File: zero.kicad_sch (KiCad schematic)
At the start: 11 parts, among them U1 Pico

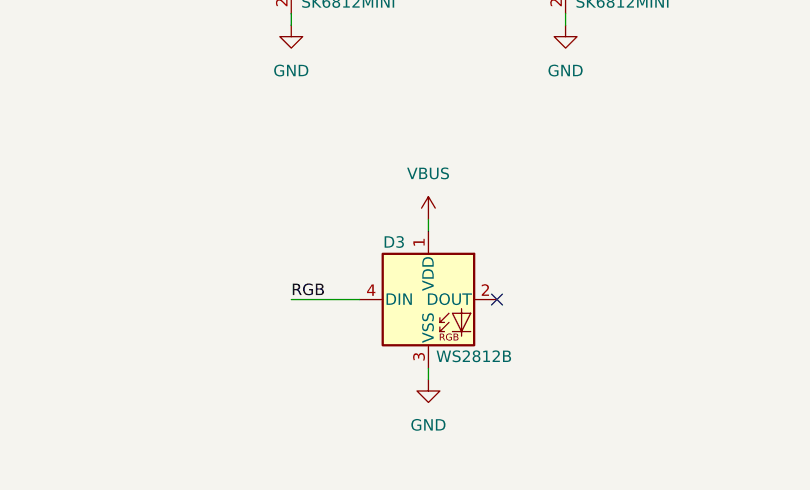
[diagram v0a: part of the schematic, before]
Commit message: Remove WS2812B
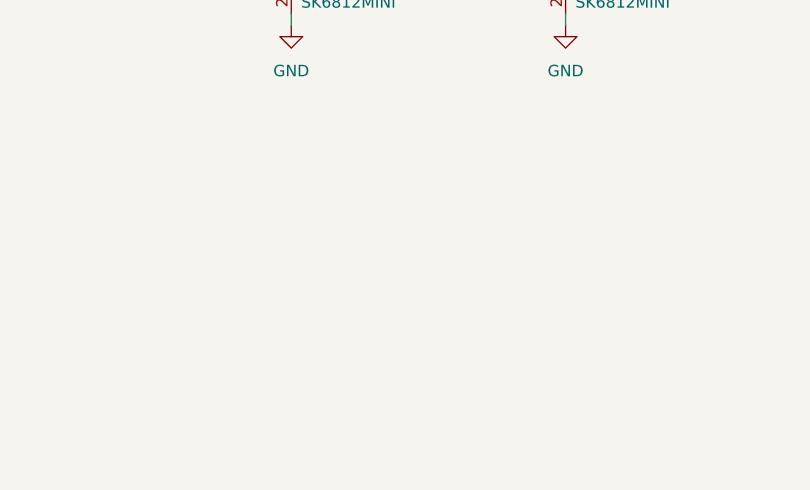
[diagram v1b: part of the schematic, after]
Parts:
- removed D3: WS2812B, LED_SMD:LED_WS2812B_PLCC4_5.0x5.0mm_P3.2mm, symbol LED:WS2812B
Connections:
- no-connect marks 29 -> 28
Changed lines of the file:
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@@
   (no_connect (at 191.77 66.04))
   (no_connect (at 227.33 66.04))
-  (no_connect (at 217.17 147.32))
   (no_connect (at 232.41 107.95))
   (no_connect (at 227.33 73.66))
@@
     (stroke (width 0) (type default) (color 0 0 0 0))
   )
-  (wire (pts (xy 209.55 154.94) (xy 209.55 156.21))
-    (stroke (width 0) (type default) (color 0 0 0 0))
-  )
   (wire (pts (xy 227.33 33.02) (xy 241.3 33.02))
     (stroke (width 0) (type default) (color 0 0 0 0))
@@
     (stroke (width 0) (type default) (color 0 0 0 0))
   )
-  (wire (pts (xy 194.31 147.32) (xy 201.93 147.32))
-    (stroke (width 0) (type default) (color 0 0 0 0))
-  )
   (wire (pts (xy 91.44 50.165) (xy 93.98 50.165))
     (stroke (width 0) (type default) (color 0 0 0 0))
@@
   )
   (wire (pts (xy 227.33 58.42) (xy 241.3 58.42))
-    (stroke (width 0) (type default) (color 0 0 0 0))
-  )
-  (wire (pts (xy 209.55 138.43) (xy 209.55 139.7))
     (stroke (width 0) (type default) (color 0 0 0 0))
   )
@@
   )
   (label "ROW6" (at 251.46 59.055 0)
-    (effects (font (size 1.27 1.27)) (justify left bottom))
-  )
-  (label "RGB" (at 194.31 147.32 0)
     (effects (font (size 1.27 1.27)) (justify left bottom))
   )
@@
     (pin "1")
   )
-  (symbol (lib_id "power:VBUS") (at 209.55 138.43 0) (unit 1)
-    (in_bom yes) (on_board yes) (fields_autoplaced)
-    (property "Reference" "#PWR0104" (id 0) (at 209.55 142.24 0)
-      (effects (font (size 1.27 1.27)) hide)
-    )
-    (property "Value" "VBUS" (id 1) (at 209.55 133.35 0))
-    (property "Footprint" "" (id 2) (at 209.55 138.43 0)
-      (effects (font (size 1.27 1.27)) hide)
-    )
-    (property "Datasheet" "" (id 3) (at 209.55 138.43 0)
-      (effects (font (size 1.27 1.27)) hide)
-    )
-    (pin "1")
-  )
   (symbol (lib_id "power:GND") (at 283.21 160.02 0) (unit 1)
     (in_bom yes) (on_board yes) (fields_autoplaced)
@@
     )
     (pin "1")
-  )
-  (symbol (lib_id "LED:WS2812B") (at 209.55 147.32 0) (unit 1)
-    (in_bom yes) (on_board yes)
-    (property "Reference" "D3" (id 0) (at 205.74 140.97 0))
-    (property "Value" "WS2812B" (id 1) (at 214.63 153.67 0))
-    (property "Footprint" "LED_SMD:LED_WS2812B_PLCC4_5.0x5.0mm_P3.2mm" (id 2) (at 210.82 154.94 0)
-      (effects (font (size 1.27 1.27)) (justify left top) hide)
-    )
-    (property "Datasheet" "https://cdn-shop.adafruit.com/datasheets/WS2812B.pdf" (id 3) (at 212.09 156.845 0)
-      (effects (font (size 1.27 1.27)) (justify left top) hide)
-    )
-    (pin "1")
-    (pin "2")
-    (pin "3")
-    (pin "4")
   )
   (symbol (lib_id "LED:SK6812MINI") (at 224.79 107.95 0) (unit 1)
@@
     )
     (property "Datasheet" "" (id 3) (at 246.38 31.75 0)
-      (effects (font (size 1.27 1.27)) hide)
-    )
-    (pin "1")
-  )
-  (symbol (lib_id "power:GND") (at 209.55 156.21 0) (unit 1)
-    (in_bom yes) (on_board yes) (fields_autoplaced)
-    (property "Reference" "#PWR0102" (id 0) (at 209.55 162.56 0)
-      (effects (font (size 1.27 1.27)) hide)
-    )
-    (property "Value" "GND" (id 1) (at 209.55 161.29 0))
-    (property "Footprint" "" (id 2) (at 209.55 156.21 0)
-      (effects (font (size 1.27 1.27)) hide)
-    )
-    (property "Datasheet" "" (id 3) (at 209.55 156.21 0)
       (effects (font (size 1.27 1.27)) hide)
     )
@@
       (reference "#PWR0101") (unit 1) (value "GND") (footprint "")
     )
-    (path "/fc1d2dd2-674a-451f-aaed-89909acb41ee"
-      (reference "#PWR0102") (unit 1) (value "GND") (footprint "")
-    )
     (path "/3afa3d3e-8cb2-411d-b44e-31bd6eef1a90"
       (reference "#PWR0103") (unit 1) (value "VBUS") (footprint "")
     )
-    (path "/402589d2-4949-4e67-ab58-84e597eda113"
-      (reference "#PWR0104") (unit 1) (value "VBUS") (footprint "")
-    )
     (path "/db1c789c-278d-4363-91f8-23280507cd39"
       (reference "#PWR0105") (unit 1) (value "VBUS") (footprint "")
@@
       (reference "D2") (unit 1) (value "SK6812MINI") (footprint "LED_SMD:LED_SK6812MINI_PLCC4_3.5x3.5mm_P1.75mm")
     )
-    (path "/6933132d-2e71-4eb1-a4da-1bd892f00f49"
-      (reference "D3") (unit 1) (value "WS2812B") (footprint "LED_SMD:LED_WS2812B_PLCC4_5.0x5.0mm_P3.2mm")
-    )
     (path "/0f942d18-8305-42c2-8896-a19741d9225a"

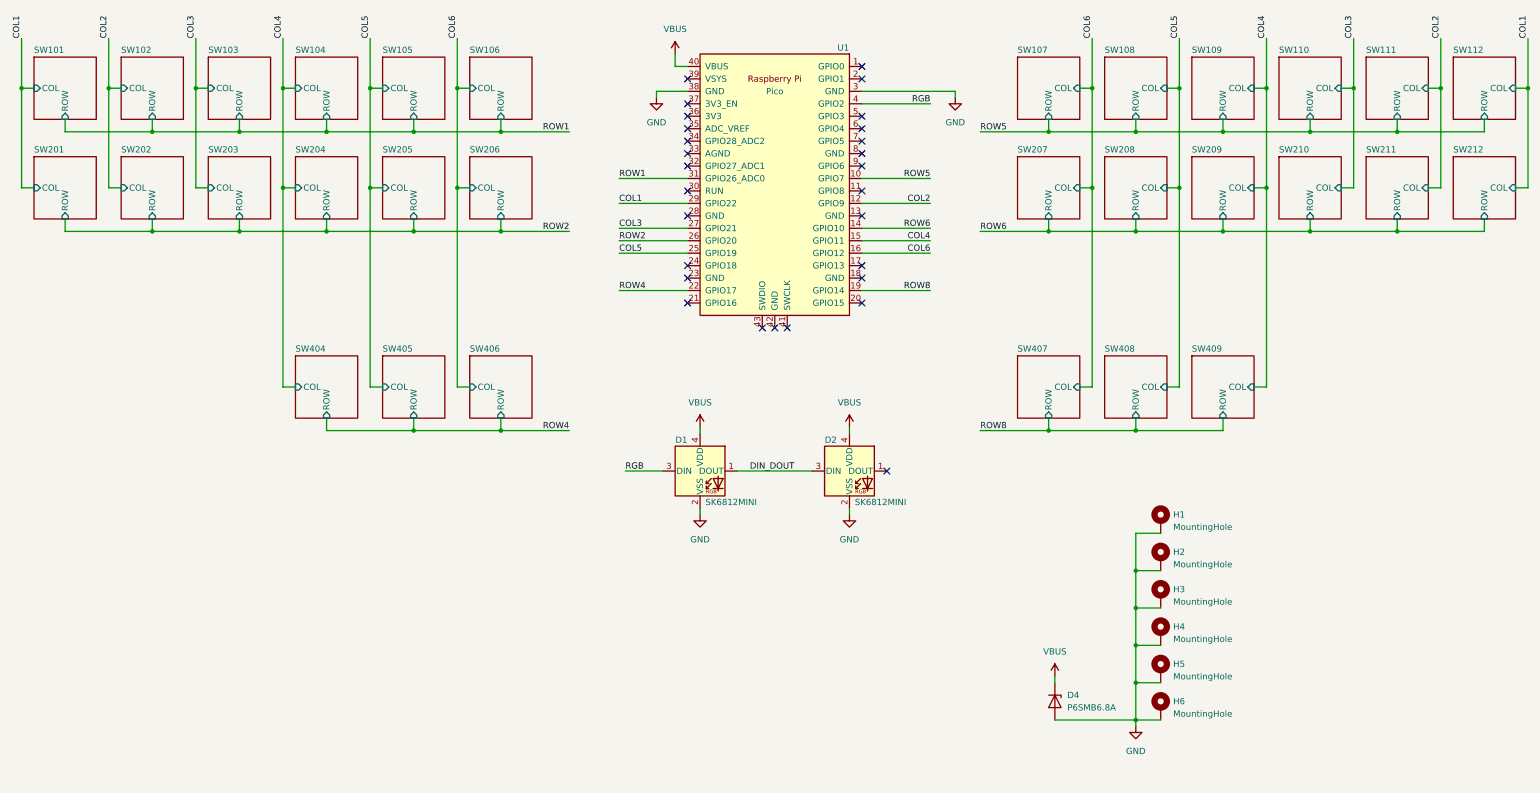
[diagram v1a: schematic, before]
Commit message: Add edge clearance for ground pours
- Change mounting holes for pico to PTHs
- Connect RGB power to VSYS instead of VBUS (this gives us more
  clearance around the mounting holes and should work equally well)
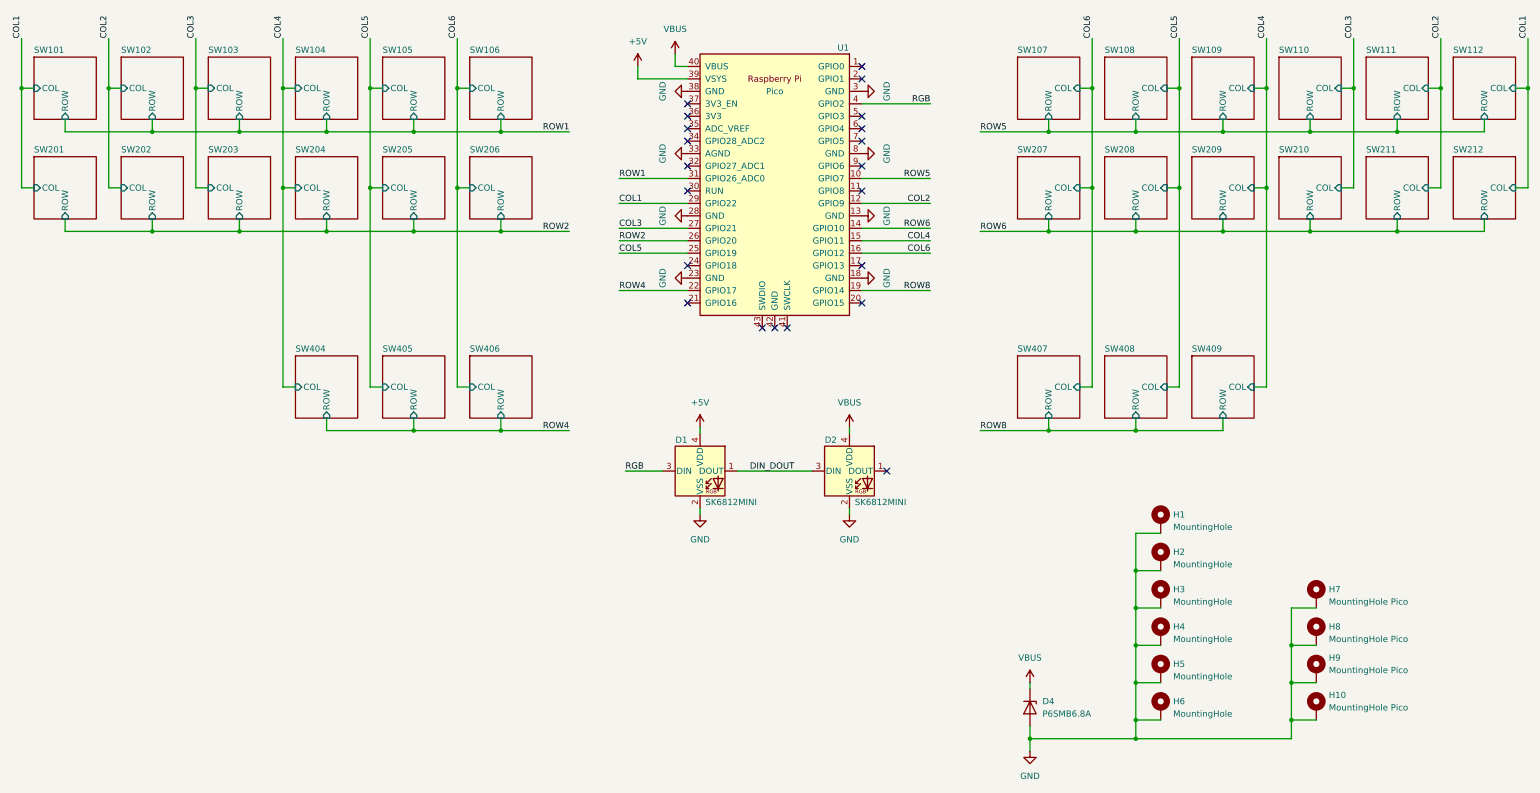
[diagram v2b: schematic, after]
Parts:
- added H10, H7, H8, H9: MountingHole Pico, footprints:M2 Hole Pico, symbol Mechanical:MountingHole_Pad
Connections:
- net GND: now also U1.13 (GND), U1.18 (GND), U1.23 (GND), U1.28 (GND), U1.33 (AGND), U1.8 (GND), H10.1, H7.1, H8.1, H9.1
- net VBUS: no longer D1.4 (VDD)
- net +5V: now reaches U1.39 (VSYS)
- net +5V: now also D1.4 (VDD)
- no-connect marks 28 -> 21
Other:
- moved on the sheet: D4

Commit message: Add logo on backside
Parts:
- added LOGO_1: CHORD LOGO, footprints:chord_logo_3d, symbol Mechanical:MountingHole_Pad
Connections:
- net GND: now also LOGO_1.1
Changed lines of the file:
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@@
   (junction (at 314.96 158.75) (diameter 0) (color 0 0 0 0)
+  )
+  (junction (at 314.96 135.89) (diameter 0) (color 0 0 0 0)
   )
   (junction (at 318.77 38.735) (diameter 0) (color 0 0 0 0)
@@
     (stroke (width 0) (type default) (color 0 0 0 0))
   )
+  (wire (pts (xy 314.96 120.65) (xy 320.04 120.65))
+    (stroke (width 0) (type default) (color 0 0 0 0))
+  )
   (wire (pts (xy 309.88 29.845) (xy 309.88 50.165))
     (stroke (width 0) (type default) (color 0 0 0 0))
@@
   )
   (wire (pts (xy 64.77 36.195) (xy 64.77 38.735))
+    (stroke (width 0) (type default) (color 0 0 0 0))
+  )
+  (wire (pts (xy 314.96 120.65) (xy 314.96 135.89))
     (stroke (width 0) (type default) (color 0 0 0 0))
   )
@@
     (pin "1")
   )
+  (symbol (lib_id "Mechanical:MountingHole_Pad") (at 320.04 118.11 0) (unit 1)
+    (in_bom yes) (on_board yes) (fields_autoplaced)
+    (property "Reference" "LOGO_1" (id 0) (at 322.58 116.8399 0)
+      (effects (font (size 1.27 1.27)) (justify left))
+    )
+    (property "Value" "CHORD LOGO" (id 1) (at 322.58 119.3799 0)
+      (effects (font (size 1.27 1.27)) (justify left))
+    )
+    (property "Footprint" "footprints:chord_logo_3d" (id 2) (at 320.04 118.11 0)
+      (effects (font (size 1.27 1.27)) hide)
+    )
+    (property "Datasheet" "~" (id 3) (at 320.04 118.11 0)
+      (effects (font (size 1.27 1.27)) hide)
+    )
+    (pin "1")
+  )
   (symbol (lib_id "power:GND") (at 191.77 30.48 270) (unit 1)
     (in_bom yes) (on_board yes)
@@
       (reference "H10") (unit 1) (value "MountingHole Pico") (footprint "footprints:M2 Hole Pico")
     )
+    (path "/207fd99f-853a-4d30-b4a3-7fae6fe9b23e"
+      (reference "LOGO_1") (unit 1) (value "CHORD LOGO") (footprint "footprints:chord_logo_3d")
+    )
     (path "/bc3939ff-dba2-4cf9-9b69-43b9ed01bab8/505156cb-1eec-4a3b-b2f0-476b9e108ade"
